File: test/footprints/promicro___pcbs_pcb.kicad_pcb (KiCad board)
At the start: 2 copper layers, 2 parts

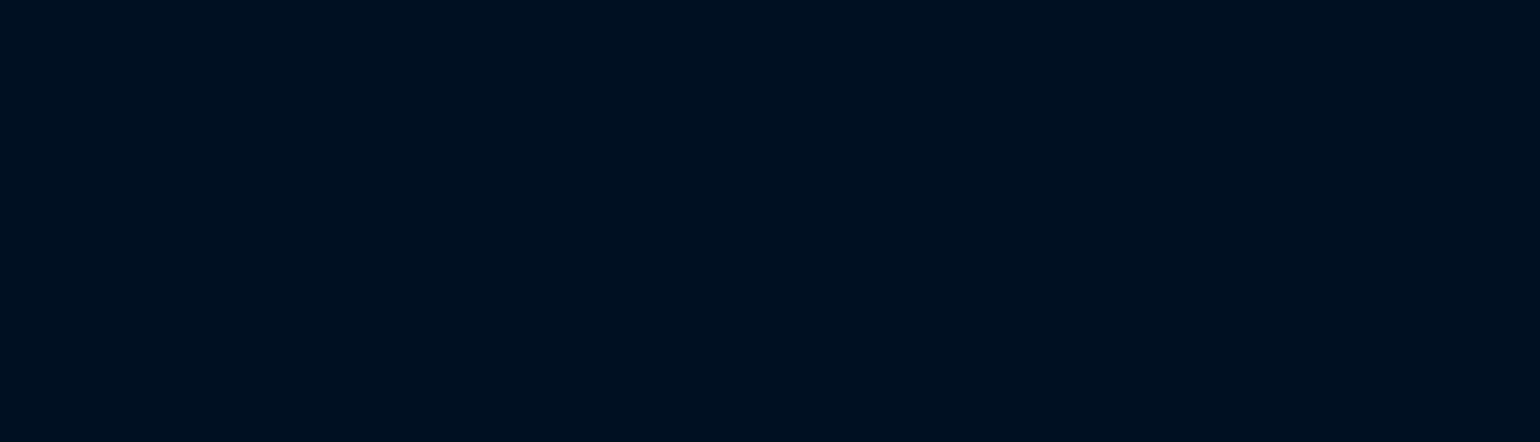
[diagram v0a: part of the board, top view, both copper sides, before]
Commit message: Add support for selecting PCB side for promicro
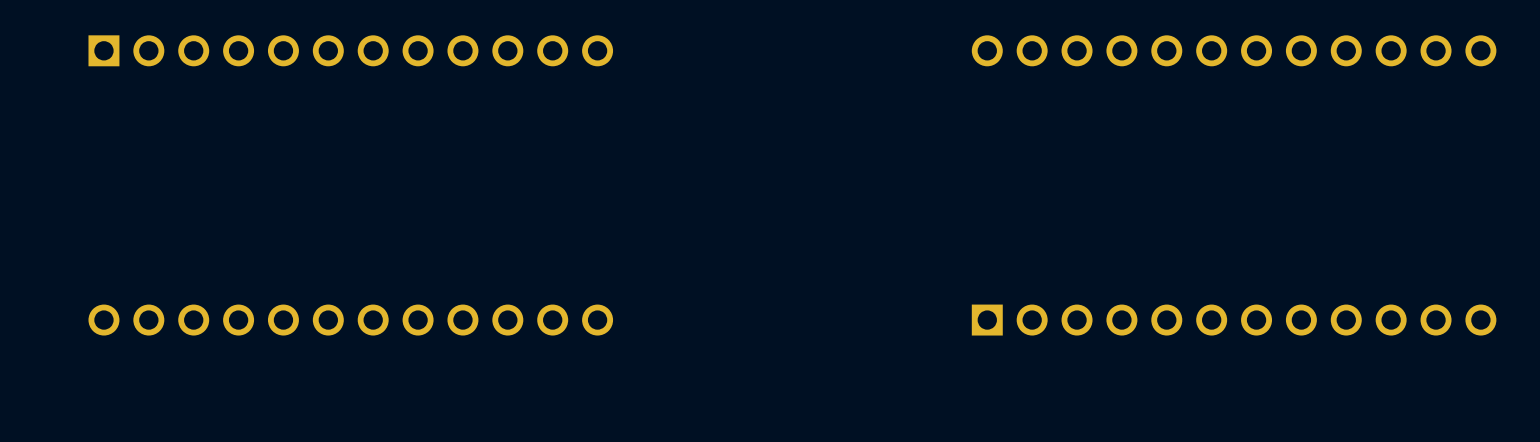
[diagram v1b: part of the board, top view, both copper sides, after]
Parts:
- added MCU3: , ProMicro, F.Cu at (0.00, -50.0)
- added MCU4: , ProMicro, F.Cu at (50.0, -50.0)
